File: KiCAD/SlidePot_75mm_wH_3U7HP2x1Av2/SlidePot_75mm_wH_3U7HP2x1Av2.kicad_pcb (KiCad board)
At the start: 2 copper layers, 35.2 x 128.5 mm, 5 parts

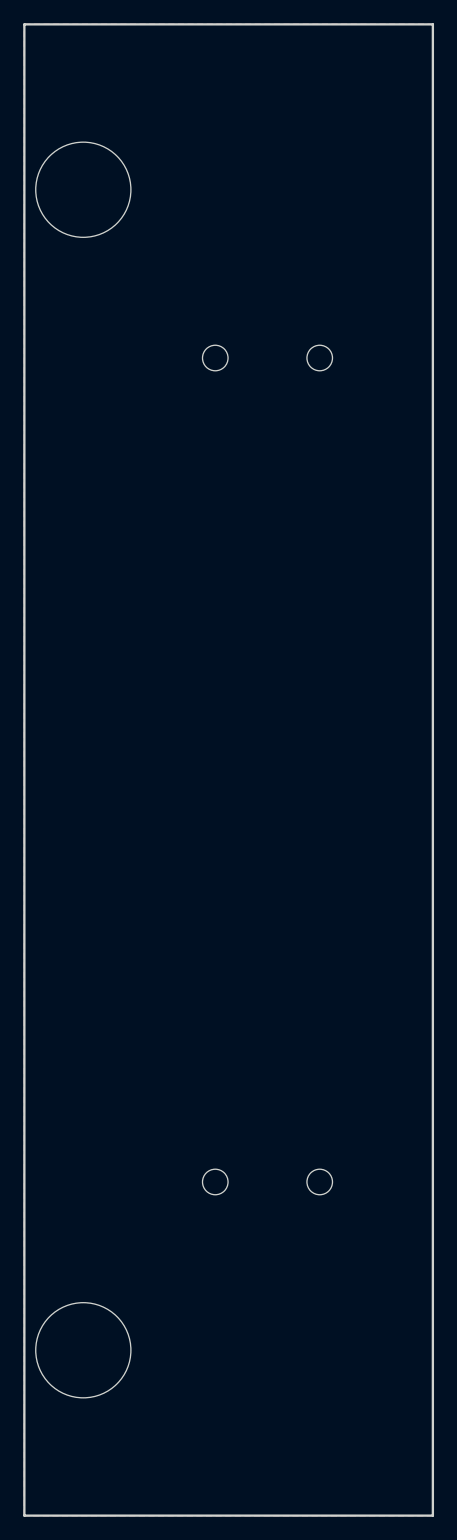
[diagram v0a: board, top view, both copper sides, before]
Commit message: updated all modules to use plated through-holes wherever possible
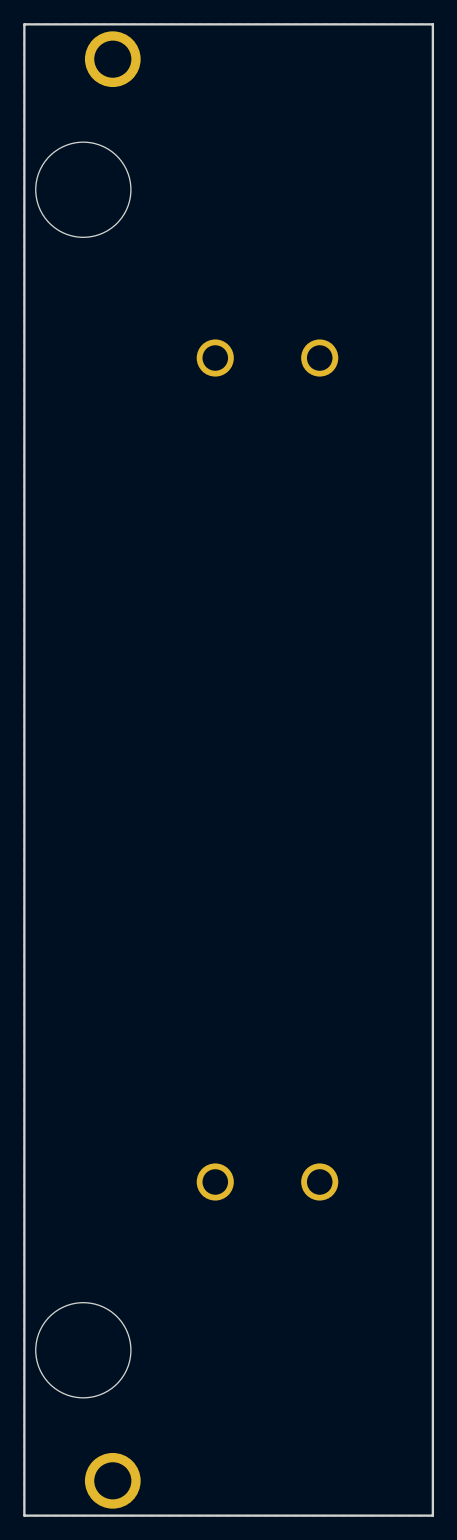
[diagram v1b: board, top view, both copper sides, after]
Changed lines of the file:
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@@
 			)
 		)
-		(pad "" np_thru_hole circle
+		(pad "" thru_hole circle
 			(at 0 -35.5)
-			(size 2.2 2.2)
+			(size 3.2 3.2)
 			(drill 2.2)
 			(layers "*.Cu" "*.Mask")
+			(remove_unused_layers no)
 		)
 		(pad "" np_thru_hole oval
@@
 			(layers "*.Cu" "*.Mask")
 		)
-		(pad "" np_thru_hole circle
+		(pad "" thru_hole circle
 			(at 0 35.5)
-			(size 2.2 2.2)
+			(size 3.2 3.2)
 			(drill 2.2)
 			(layers "*.Cu" "*.Mask")
+			(remove_unused_layers no)
 		)
 		(embedded_fonts no)
@@
 			)
 		)
-		(pad "" np_thru_hole circle
+		(pad "" thru_hole circle
 			(at 0 -35.5)
-			(size 2.2 2.2)
+			(size 3.2 3.2)
 			(drill 2.2)
 			(layers "*.Cu" "*.Mask")
+			(remove_unused_layers no)
 		)
 		(pad "" np_thru_hole oval
@@
 			(layers "*.Cu" "*.Mask")
 		)
-		(pad "" np_thru_hole circle
+		(pad "" thru_hole circle
 			(at 0 35.5)
-			(size 2.2 2.2)
+			(size 3.2 3.2)
 			(drill 2.2)
 			(layers "*.Cu" "*.Mask")
+			(remove_unused_layers no)
 		)
 		(embedded_fonts no)
@@
 			)
 		)
-		(pad "" np_thru_hole oval
+		(pad "" thru_hole circle
 			(at 0 0)
-			(size 4.34 3.2)
-			(drill oval 4.34 3.2)
-			(layers "*.Cu" "*.Mask")
+			(size 4.8 4.8)
+			(drill 3.2)
+			(layers "*.Cu" "*.Mask")
+			(remove_unused_layers no)
 		)
 		(embedded_fonts no)
@@
 			)
 		)
-		(pad "" np_thru_hole oval
+		(pad "" thru_hole circle
 			(at 0 0)
-			(size 4.34 3.2)
-			(drill oval 4.34 3.2)
-			(layers "*.Cu" "*.Mask")
+			(size 4.8 4.8)
+			(drill 3.2)
+			(layers "*.Cu" "*.Mask")
+			(remove_unused_layers no)
 		)
 		(embedded_fonts no)
